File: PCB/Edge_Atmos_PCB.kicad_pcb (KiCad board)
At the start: 2 copper layers, 7 parts, among them J1 AHT10, J2 BMP280, J3 W25Q32, J4 STM32F103C8T6_1, J5 STM32F103C8T6_2, J6 TFT, J7 Conn_01x04

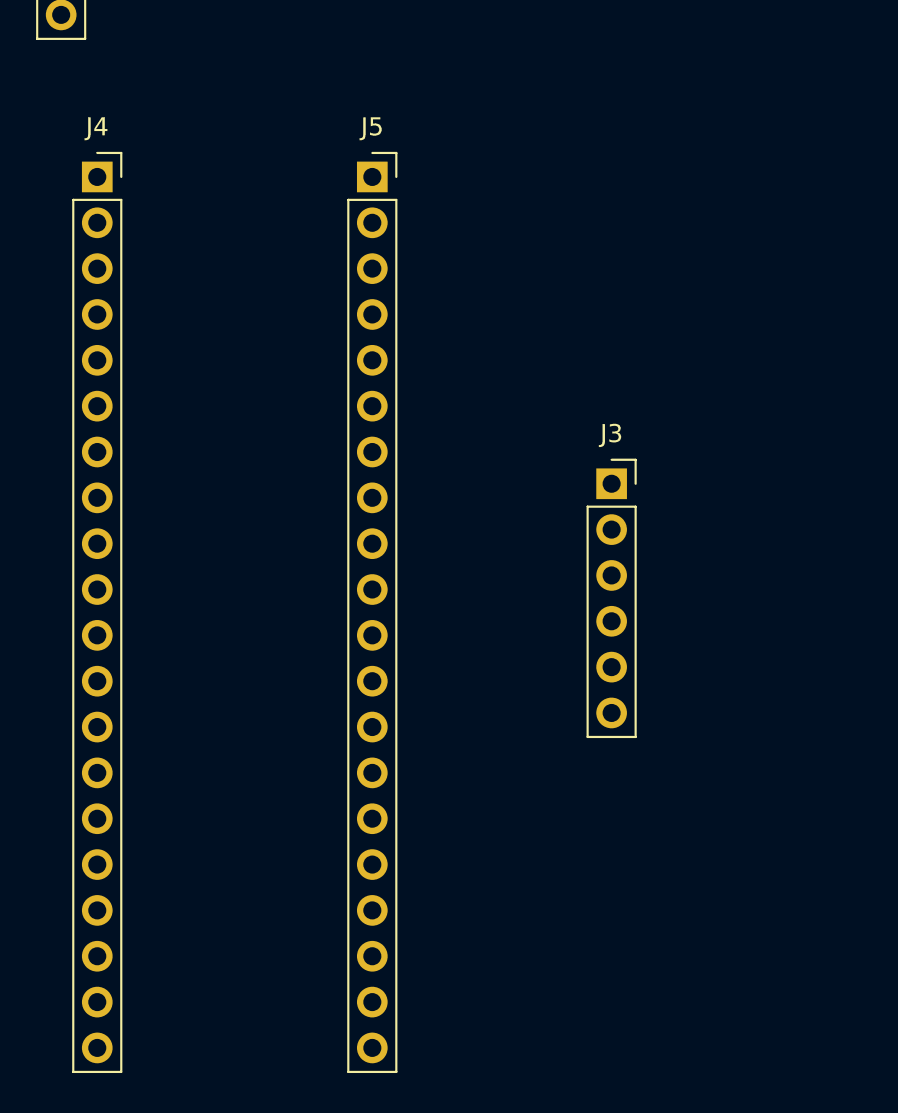
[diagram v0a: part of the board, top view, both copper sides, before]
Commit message: Increased number of windows
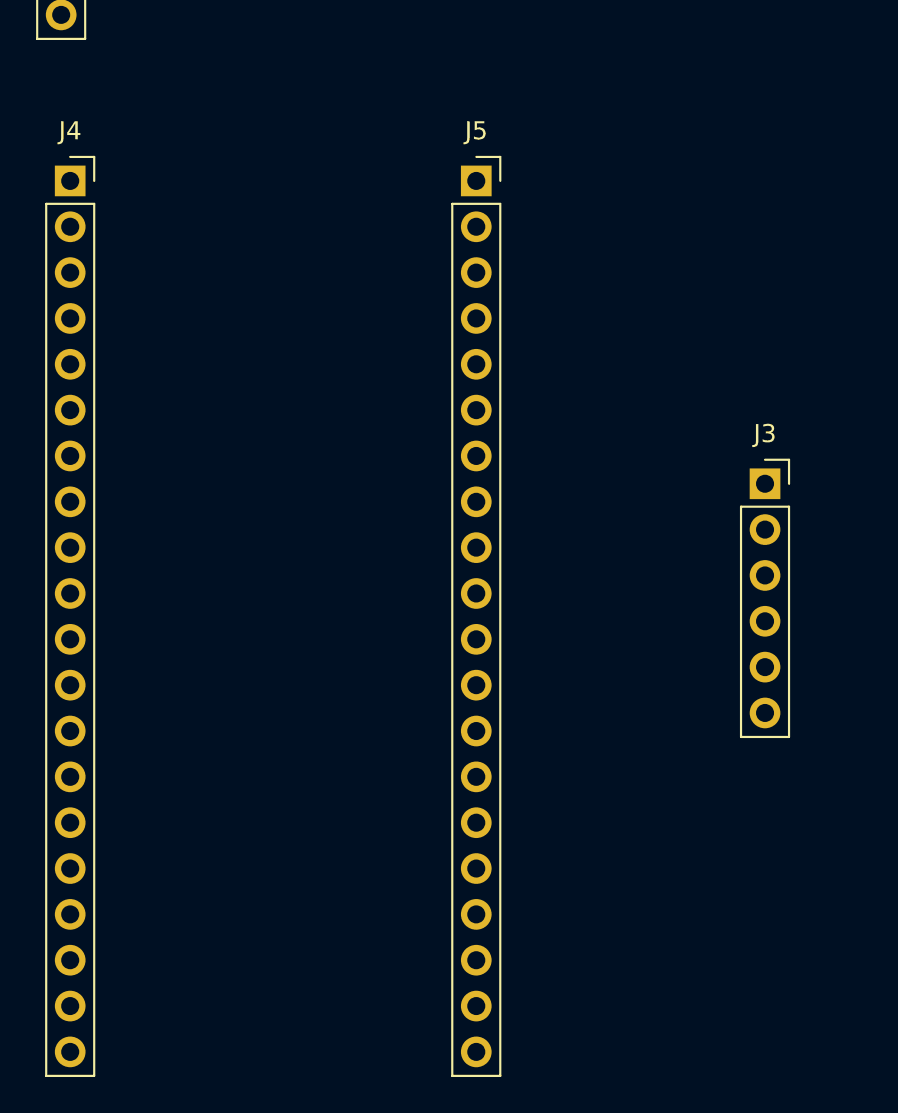
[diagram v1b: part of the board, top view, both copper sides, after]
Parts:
- moved J3 8.50 mm to (141.0, 120.2)
- moved J5 5.76 mm to (125.0, 103.4)
- moved J4 1.52 mm to (102.5, 103.4)
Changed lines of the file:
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@@
 	(footprint "Connector_PinSocket_2.54mm:PinSocket_1x20_P2.54mm_Vertical"
 		(layer "F.Cu")
-		(at 104 103.18)
+		(at 102.5 103.4)
 		(descr "Through hole straight socket strip, 1x20, 2.54mm pitch, single row (from Kicad 4.0.7), script generated")
 		(tags "Through hole socket strip THT 1x20 2.54mm single row")
@@
 	(footprint "Connector_PinSocket_2.54mm:PinSocket_1x06_P2.54mm_Vertical"
 		(layer "F.Cu")
-		(at 132.5 120.18)
+		(at 141 120.18)
 		(descr "Through hole straight socket strip, 1x06, 2.54mm pitch, single row (from Kicad 4.0.7), script generated")
 		(tags "Through hole socket strip THT 1x06 2.54mm single row")
@@
 	(footprint "Connector_PinSocket_2.54mm:PinSocket_1x20_P2.54mm_Vertical"
 		(layer "F.Cu")
-		(at 119.24 103.18)
+		(at 125 103.4)
 		(descr "Through hole straight socket strip, 1x20, 2.54mm pitch, single row (from Kicad 4.0.7), script generated")
 		(tags "Through hole socket strip THT 1x20 2.54mm single row")
